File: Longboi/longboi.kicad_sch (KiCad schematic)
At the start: 192 parts, among them J2 ICSP_Header, K0 KEYSW, K1 KEYSW, K10 KEYSW, K11 KEYSW, K12 KEYSW, K13 KEYSW, K14 KEYSW, K15 KEYSW, K16 KEYSW, K17 KEYSW, K18 KEYSW, K19 KEYSW, K2 KEYSW, K20 KEYSW, K21 KEYSW, K22 KEYSW, K22-spacer1 KEYSW, K22-stepped1 KEYSW, K23 KEYSW, K24 KEYSW, K25 KEYSW, K26 KEYSW, K27 KEYSW, K28 KEYSW, K29 KEYSW, K3 KEYSW, K3-2uVert1 KEYSW, K30 KEYSW, K31 KEYSW, K32 KEYSW, K33 KEYSW, K34 KEYSW, K35 KEYSW, K36 KEYSW, K37 KEYSW, K38 KEYSW, K38-2uVert1 KEYSW, K39 KEYSW, K39-spacer1 KEYSW, K4 KEYSW, K4-spacer1 KEYSW, K40 KEYSW, K41 KEYSW, K42 KEYSW, K43 KEYSW, K44 KEYSW, K45 KEYSW, K46 KEYSW, K47 KEYSW, K48 KEYSW, K49 KEYSW, K5 KEYSW, K50 KEYSW, K51 KEYSW, K52 KEYSW, K52-1u1 KEYSW, K52-2u1 KEYSW, K53 KEYSW, K54 KEYSW, K55 KEYSW, K55-1.25 KEYSW, K55-spacer1 KEYSW, K56 KEYSW, K56-1.25 KEYSW, K57 KEYSW, K57-1.25 KEYSW, K57-1.5u1 KEYSW, K57-1u1 KEYSW, K58 KEYSW, K58-6u1 KEYSW, K58for1.25Row1 KEYSW, K59 KEYSW, K59-1.25u1 KEYSW, K59-7u1 KEYSW, K59Alt1 KEYSW, K6 KEYSW, K60 KEYSW, K60Alt1 KEYSW, K61 KEYSW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

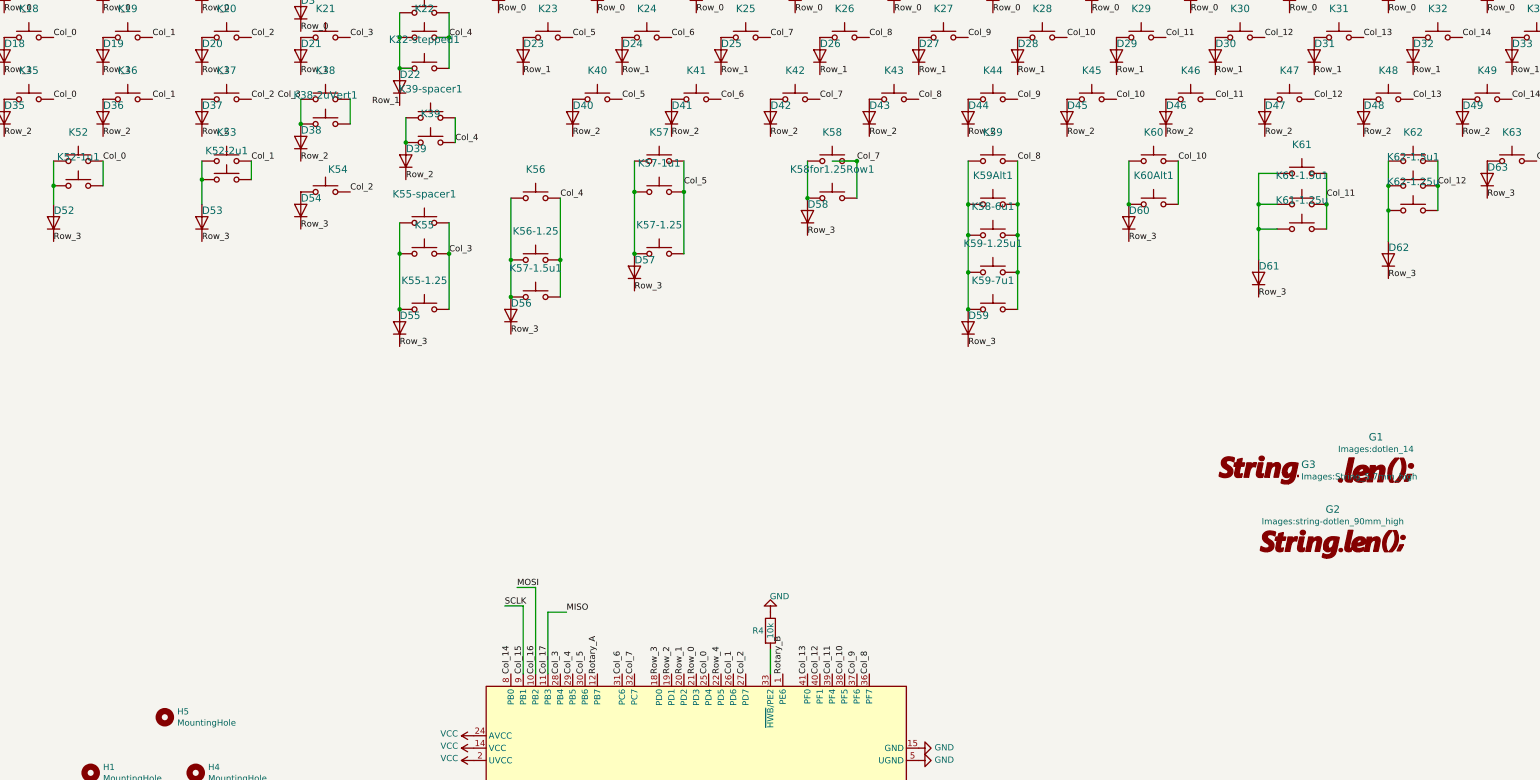
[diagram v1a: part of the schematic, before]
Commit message: fix bug in longboi...
key38 was not schematiced right
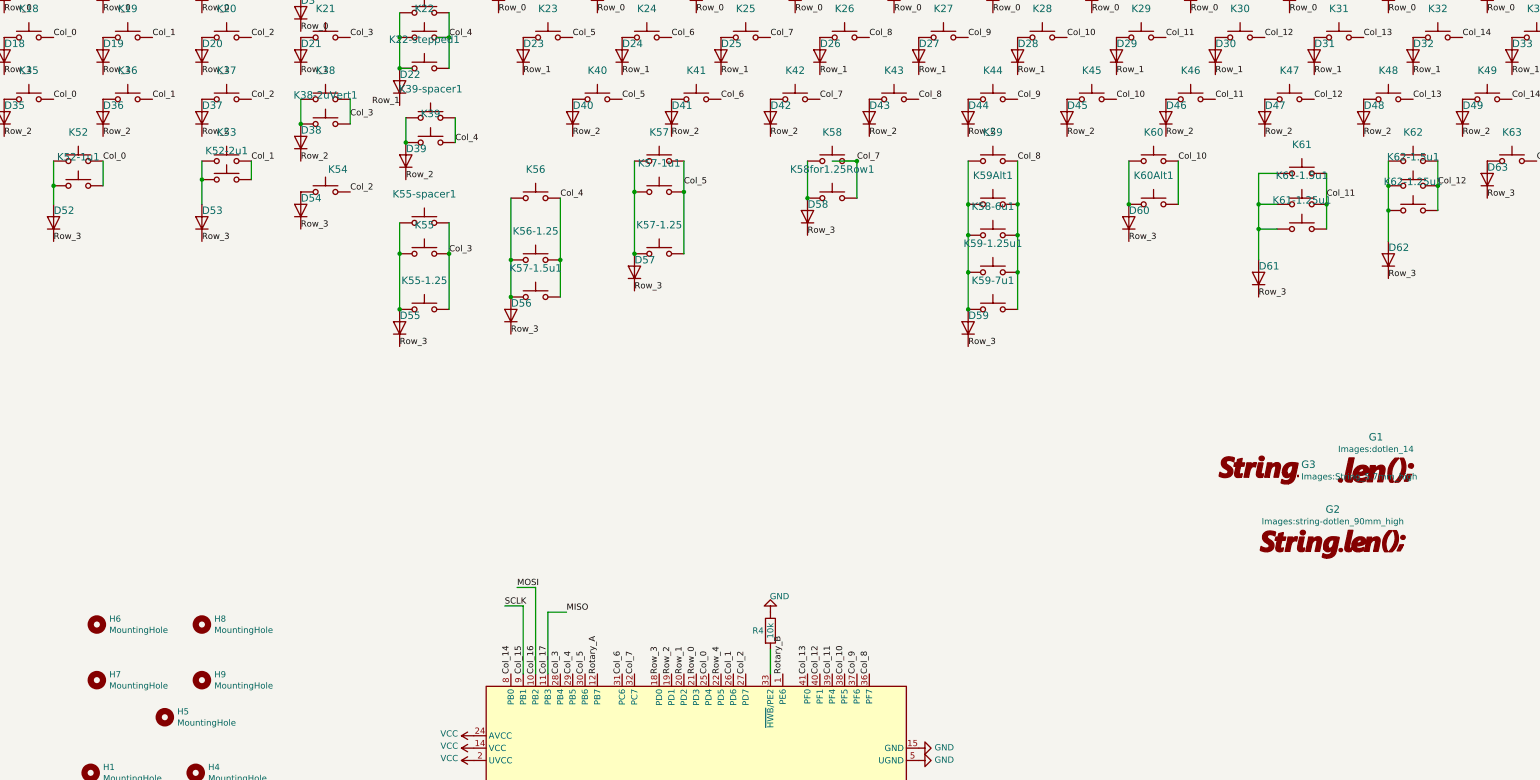
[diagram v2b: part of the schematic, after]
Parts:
- added H6, H7, H8, H9: MountingHole, random-keyboard-parts:M2 Mounting Hole, symbol Mechanical:MountingHole
- renumbered K61-1.25u to K61-1.25u1, K62-1.25u to K62-1.25u1
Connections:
- net Col_3: now also K38-2uVert1.2, K38.2; no longer D38.2 (A), K38-2uVert1.1, K38.1
- new net: D38.2 (A), K38-2uVert1.1, K38.1
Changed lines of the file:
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@@
   (junction (at 185.42 90.17) (diameter 0) (color 0 0 0 0)
   )
-  (junction (at 81.28 74.93) (diameter 0) (color 0 0 0 0)
-  )
   (junction (at 111.76 101.6) (diameter 0) (color 0 0 0 0)
   )
@@
   (junction (at 69.85 242.57) (diameter 0) (color 0 0 0 0)
   )
+  (junction (at 81.28 74.93) (diameter 0) (color 0 0 0 0)
+  )
   (junction (at 251.46 91.44) (diameter 0) (color 0 0 0 0)
   )
@@
     (stroke (width 0) (type default) (color 0 0 0 0))
   )
-  (wire (pts (xy 81.28 69.85) (xy 81.28 74.93))
-    (stroke (width 0) (type default) (color 0 0 0 0))
-  )
   (wire (pts (xy 190.5 82.55) (xy 195.58 82.55))
     (stroke (width 0) (type default) (color 0 0 0 0))
@@
     (stroke (width 0) (type default) (color 0 0 0 0))
   )
+  (wire (pts (xy 81.28 69.85) (xy 81.28 74.93))
+    (stroke (width 0) (type default) (color 0 0 0 0))
+  )
   (wire (pts (xy 394.97 36.83) (xy 403.86 36.83))
     (stroke (width 0) (type default) (color 0 0 0 0))
@@
     (effects (font (size 1.27 1.27)) (justify left bottom))
   )
-  (label "Col_3" (at 81.28 69.85 180)
-    (effects (font (size 1.27 1.27)) (justify right bottom))
+  (label "Col_3" (at 91.44 73.66 0)
+    (effects (font (size 1.27 1.27)) (justify left bottom))
   )
   (label "Row_1" (at 269.24 64.77 0)
@@
     (pin "2")
   )
+  (symbol (lib_id "Mechanical:MountingHole") (at 39.37 189.23 0) (unit 1)
+    (in_bom yes) (on_board yes)
+    (property "Reference" "H7" (id 0) (at 41.91 188.0616 0)
+      (effects (font (size 1.27 1.27)) (justify left))
+    )
+    (property "Value" "MountingHole" (id 1) (at 41.91 190.373 0)
+      (effects (font (size 1.27 1.27)) (justify left))
+    )
+    (property "Footprint" "random-keyboard-parts:M2 Mounting Hole" (id 2) (at 39.37 189.23 0)
+      (effects (font (size 1.27 1.27)) hide)
+    )
+    (property "Datasheet" "~" (id 3) (at 39.37 189.23 0)
+      (effects (font (size 1.27 1.27)) hide)
+    )
+  )
+  (symbol (lib_id "Mechanical:MountingHole") (at 60.96 177.8 0) (unit 1)
+    (in_bom yes) (on_board yes)
+    (property "Reference" "H8" (id 0) (at 63.5 176.6316 0)
+      (effects (font (size 1.27 1.27)) (justify left))
+    )
+    (property "Value" "MountingHole" (id 1) (at 63.5 178.943 0)
+      (effects (font (size 1.27 1.27)) (justify left))
+    )
+    (property "Footprint" "random-keyboard-parts:M2 Mounting Hole" (id 2) (at 60.96 177.8 0)
+      (effects (font (size 1.27 1.27)) hide)
+    )
+    (property "Datasheet" "~" (id 3) (at 60.96 177.8 0)
+      (effects (font (size 1.27 1.27)) hide)
+    )
+  )
+  (symbol (lib_id "Mechanical:MountingHole") (at 60.96 189.23 0) (unit 1)
+    (in_bom yes) (on_board yes)
+    (property "Reference" "H9" (id 0) (at 63.5 188.0616 0)
+      (effects (font (size 1.27 1.27)) (justify left))
+    )
+    (property "Value" "MountingHole" (id 1) (at 63.5 190.373 0)
+      (effects (font (size 1.27 1.27)) (justify left))
+    )
+    (property "Footprint" "random-keyboard-parts:M2 Mounting Hole" (id 2) (at 60.96 189.23 0)
+      (effects (font (size 1.27 1.27)) hide)
+    )
+    (property "Datasheet" "~" (id 3) (at 60.96 189.23 0)
+      (effects (font (size 1.27 1.27)) hide)
+    )
+  )
   (symbol (lib_id "Switch:SW_Push") (at 309.88 92.71 0) (unit 1)
     (in_bom yes) (on_board yes)
-    (property "Reference" "K62-1.25u" (id 0) (at 309.88 86.7918 0)
+    (property "Reference" "K62-1.25u1" (id 0) (at 309.88 86.7918 0)
       (effects (font (size 1.524 1.524)))
     )
@@
   (symbol (lib_id "Switch:SW_Push") (at 287.02 96.52 0) (unit 1)
     (in_bom yes) (on_board yes)
-    (property "Reference" "K61-1.25u" (id 0) (at 287.02 90.6018 0)
+    (property "Reference" "K61-1.25u1" (id 0) (at 287.02 90.6018 0)
       (effects (font (size 1.524 1.524)))
     )
@@
     (pin "2")
   )
+  (symbol (lib_id "Mechanical:MountingHole") (at 39.37 177.8 0) (unit 1)
+    (in_bom yes) (on_board yes)
+    (property "Reference" "H6" (id 0) (at 41.91 176.6316 0)
+      (effects (font (size 1.27 1.27)) (justify left))
+    )
+    (property "Value" "MountingHole" (id 1) (at 41.91 178.943 0)
+      (effects (font (size 1.27 1.27)) (justify left))
+    )
+    (property "Footprint" "random-keyboard-parts:M2 Mounting Hole" (id 2) (at 39.37 177.8 0)
+      (effects (font (size 1.27 1.27)) hide)
+    )
+    (property "Datasheet" "~" (id 3) (at 39.37 177.8 0)
+      (effects (font (size 1.27 1.27)) hide)
+    )
+  )
   (symbol (lib_id "Switch:SW_Push") (at 66.04 86.36 0) (unit 1)
     (in_bom yes) (on_board yes)
@@
       (reference "H5") (unit 1) (value "MountingHole") (footprint "random-keyboard-parts:M2 Mounting Hole")
     )
+    (path "/e0ffc4a5-acee-444d-9091-cb09a2fd596a"
+      (reference "H6") (unit 1) (value "MountingHole") (footprint "random-keyboard-parts:M2 Mounting Hole")
+    )
+    (path "/10fcbf2d-6552-4910-ae9e-906304f0e093"
+      (reference "H7") (unit 1) (value "MountingHole") (footprint "random-keyboard-parts:M2 Mounting Hole")
+    )
+    (path "/339b77fe-16f3-43b4-8399-7230a8ae2102"
+      (reference "H8") (unit 1) (value "MountingHole") (footprint "random-keyboard-parts:M2 Mounting Hole")
+    )
+    (path "/3427d123-61e2-4c57-80e1-efb5d2751d47"
+      (reference "H9") (unit 1) (value "MountingHole") (footprint "random-keyboard-parts:M2 Mounting Hole")
+    )
     (path "/00000000-0000-0000-0000-000062166a49"
       (reference "J2") (unit 1) (value "ICSP_Header") (footprint "Connector_PinHeader_2.54mm:PinHeader_2x03_P2.54mm_Vertical")
@@
     )
     (path "/94c26993-bb91-483b-ab9b-cc98b43c45dd"
-      (reference "K61-1.25u") (unit 1) (value "KEYSW") (footprint "MX_Only:MXOnly-1.25U-NoLED")
+      (reference "K61-1.25u1") (unit 1) (value "KEYSW") (footprint "MX_Only:MXOnly-1.25U-NoLED")
     )
     (path "/00000000-0000-0000-0000-000062166a78"
@@
     )
     (path "/710abe27-ce29-434f-9460-1c18893d781d"
-      (reference "K62-1.25u") (unit 1) (value "KEYSW") (footprint "MX_Only:MXOnly-1.25U-NoLED")
+      (reference "K62-1.25u1") (unit 1) (value "KEYSW") (footprint "MX_Only:MXOnly-1.25U-NoLED")
     )
     (path "/00000000-0000-0000-0000-000062166a74"

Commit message: clean up map and string with prototype fixes
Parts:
- added D70: SOD-323F, Diode_SMD:D_SOD-323F, symbol Device:D
- added K55-spacer2, K70: KEYSW, MX_Only:MXOnly-1U-NoLED, symbol Switch:SW_Push
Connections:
- net Col_1: now also K70.2; no longer K52-2u1.2, K53.2
- net Col_2: now also K52-2u1.2, K53.2; no longer K54.2
- net Col_3: now also K54.2; no longer K55-1.25.2, K55-spacer1.2, K55.2
- net Col_4: now also K55-1.25.2, K55-spacer1.2, K55.2, K55-spacer2.2; no longer K56-1.25.2, K56.2, K57-1.5u1.2
- net Col_5: now also K56-1.25.2, K56.2, K57-1.5u1.2; no longer K57-1.25.2, K57-1u1.2, K57.2
- net Col_6: now also K57-1.25.2, K57-1u1.2, K57.2
- net Row_3: now also D70.1 (K)
- net at D55.2 (A), K55-1.25.1, K55-spacer1.1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: now also K55-spacer2.1
- new net: D70.2 (A), K70.1
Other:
- moved on the sheet: D0, D1, D10, D11, D12, D13, D14, D15, D16, D17, D18, D19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

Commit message: moreupdates to tweak the two keyboards
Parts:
- removed K52-2u1: KEYSW, MX_Only:MXOnly-2U-ReversedStabilizers-NoLED, symbol Switch:SW_Push
- added K0-2uVert1, K35-2uVert1: KEYSW, MX_Only:MXOnly-2U-NoLED, symbol Switch:SW_Push
- added K54-2u1, K70-2u1: KEYSW, MX_Only:MXOnly-2U-ReversedStabilizers-NoLED, symbol Switch:SW_Push
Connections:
- net Col_0: now also K0-2uVert1.2, K35-2uVert1.2
- net Col_1: now also K70-2u1.2
- net Col_3: now also K54-2u1.2
- net at D54.2 (A), K54.1: now also K54-2u1.1
- net at D35.2 (A), K35.1: now also K35-2uVert1.1
- net at D0.2 (A), K0.1: now also K0-2uVert1.1
- net at D70.2 (A), K70.1: now also K70-2u1.1
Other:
- moved on the sheet: K53
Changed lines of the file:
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@@
   (junction (at 342.9 40.64) (diameter 0) (color 0 0 0 0)
   )
+  (junction (at 20.32 33.02) (diameter 0) (color 0 0 0 0)
+  )
   (junction (at 242.57 102.87) (diameter 0) (color 0 0 0 0)
   )
@@
   (junction (at 287.02 142.24) (diameter 0) (color 0 0 0 0)
   )
+  (junction (at 63.5 148.59) (diameter 0) (color 0 0 0 0)
+  )
   (junction (at 104.14 156.21) (diameter 0) (color 0 0 0 0)
   )
+  (junction (at 104.14 148.59) (diameter 0) (color 0 0 0 0)
+  )
   (junction (at 167.64 135.89) (diameter 0) (color 0 0 0 0)
   )
@@
   (junction (at 63.5 156.21) (diameter 0) (color 0 0 0 0)
   )
+  (junction (at 33.02 95.25) (diameter 0) (color 0 0 0 0)
+  )
   (junction (at 163.83 78.74) (diameter 0) (color 0 0 0 0)
   )
@@
   (junction (at 123.19 247.65) (diameter 0) (color 0 0 0 0)
   )
-  (junction (at 86.36 143.51) (diameter 0) (color 0 0 0 0)
-  )
   (junction (at 204.47 78.74) (diameter 0) (color 0 0 0 0)
   )
@@
     (stroke (width 0) (type default) (color 0 0 0 0))
   )
+  (wire (pts (xy 114.3 146.05) (xy 114.3 148.59))
+    (stroke (width 0) (type default) (color 0 0 0 0))
+  )
   (wire (pts (xy 241.3 156.21) (xy 260.35 156.21))
     (stroke (width 0) (type default) (color 0 0 0 0))
@@
     (stroke (width 0) (type default) (color 0 0 0 0))
   )
+  (wire (pts (xy 63.5 146.05) (xy 63.5 148.59))
+    (stroke (width 0) (type default) (color 0 0 0 0))
+  )
   (wire (pts (xy 213.36 118.11) (xy 213.36 127))
     (stroke (width 0) (type default) (color 0 0 0 0))
@@
     (stroke (width 0) (type default) (color 0 0 0 0))
   )
+  (wire (pts (xy 30.48 29.21) (xy 30.48 33.02))
+    (stroke (width 0) (type default) (color 0 0 0 0))
+  )
   (wire (pts (xy 204.47 78.74) (xy 224.79 78.74))
     (stroke (width 0) (type default) (color 0 0 0 0))
@@
     (stroke (width 0) (type default) (color 0 0 0 0))
   )
-  (wire (pts (xy 86.36 148.59) (xy 86.36 143.51))
+  (wire (pts (xy 86.36 146.05) (xy 86.36 148.59))
     (stroke (width 0) (type default) (color 0 0 0 0))
   )
@@
     (stroke (width 0) (type default) (color 0 0 0 0))
   )
+  (wire (pts (xy 20.32 29.21) (xy 20.32 33.02))
+    (stroke (width 0) (type default) (color 0 0 0 0))
+  )
   (wire (pts (xy 394.97 33.02) (xy 394.97 36.83))
     (stroke (width 0) (type default) (color 0 0 0 0))
@@
     (stroke (width 0) (type default) (color 0 0 0 0))
   )
-  (wire (pts (xy 96.52 139.7) (xy 96.52 143.51))
-    (stroke (width 0) (type default) (color 0 0 0 0))
-  )
   (wire (pts (xy 102.87 59.69) (xy 102.87 64.77))
     (stroke (width 0) (type default) (color 0 0 0 0))
@@
     (stroke (width 0) (type default) (color 0 0 0 0))
   )
+  (wire (pts (xy 73.66 146.05) (xy 73.66 148.59))
+    (stroke (width 0) (type default) (color 0 0 0 0))
+  )
   (wire (pts (xy 331.47 156.21) (xy 351.79 156.21))
     (stroke (width 0) (type default) (color 0 0 0 0))
@@
     (stroke (width 0) (type default) (color 0 0 0 0))
   )
+  (wire (pts (xy 43.18 91.44) (xy 43.18 95.25))
+    (stroke (width 0) (type default) (color 0 0 0 0))
+  )
   (wire (pts (xy 241.3 148.59) (xy 241.3 139.7))
     (stroke (width 0) (type default) (color 0 0 0 0))
@@
     (stroke (width 0) (type default) (color 0 0 0 0))
   )
+  (wire (pts (xy 104.14 146.05) (xy 104.14 148.59))
+    (stroke (width 0) (type default) (color 0 0 0 0))
+  )
   (wire (pts (xy 403.86 21.59) (xy 384.81 21.59))
     (stroke (width 0) (type default) (color 0 0 0 0))
@@
     (stroke (width 0) (type default) (color 0 0 0 0))
   )
-  (wire (pts (xy 86.36 143.51) (xy 86.36 139.7))
-    (stroke (width 0) (type default) (color 0 0 0 0))
-  )
   (wire (pts (xy 403.86 30.48) (xy 403.86 21.59))
     (stroke (width 0) (type default) (color 0 0 0 0))
@@
     (stroke (width 0) (type default) (color 0 0 0 0))
   )
+  (wire (pts (xy 33.02 91.44) (xy 33.02 95.25))
+    (stroke (width 0) (type default) (color 0 0 0 0))
+  )
   (wire (pts (xy 129.54 170.18) (xy 125.73 170.18))
     (stroke (width 0) (type default) (color 0 0 0 0))
@@
     (effects (font (size 1.27 1.27)) (justify left bottom))
   )
-  (label "Col_2" (at 96.52 139.7 0)
+  (label "Col_2" (at 96.52 146.05 0)
     (effects (font (size 1.27 1.27)) (justify left bottom))
   )
@@
     (pin "2")
   )
-  (symbol (lib_id "Switch:SW_Push") (at 91.44 139.7 0) (unit 1)
+  (symbol (lib_id "Switch:SW_Push") (at 91.44 146.05 0) (unit 1)
     (in_bom yes) (on_board yes)
-    (property "Reference" "K53" (id 0) (at 91.44 133.7818 0)
+    (property "Reference" "K53" (id 0) (at 91.44 140.1318 0)
       (effects (font (size 1.524 1.524)))
     )
-    (property "Value" "KEYSW" (id 1) (at 91.44 142.24 0)
+    (property "Value" "KEYSW" (id 1) (at 91.44 148.59 0)
       (effects (font (size 1.524 1.524)) hide)
     )
-    (property "Footprint" "MX_Only:MXOnly-1U-NoLED" (id 2) (at 91.44 139.7 0)
+    (property "Footprint" "MX_Only:MXOnly-1U-NoLED" (id 2) (at 91.44 146.05 0)
       (effects (font (size 1.524 1.524)) hide)
     )
-    (property "Datasheet" "" (id 3) (at 91.44 139.7 0)
+    (property "Datasheet" "" (id 3) (at 91.44 146.05 0)
       (effects (font (size 1.524 1.524)))
     )
@@
     )
   )
+  (symbol (lib_id "Switch:SW_Push") (at 68.58 146.05 0) (unit 1)
+    (in_bom yes) (on_board yes)
+    (property "Reference" "K70-2u1" (id 0) (at 68.58 140.1318 0)
+      (effects (font (size 1.524 1.524)))
+    )
+    (property "Value" "KEYSW" (id 1) (at 68.58 148.59 0)
+      (effects (font (size 1.524 1.524)) hide)
+    )
+    (property "Footprint" "MX_Only:MXOnly-2U-ReversedStabilizers-NoLED" (id 2) (at 68.58 146.05 0)
+      (effects (font (size 1.524 1.524)) hide)
+    )
+    (property "Datasheet" "" (id 3) (at 68.58 146.05 0)
+      (effects (font (size 1.524 1.524)))
+    )
+    (pin "1")
+    (pin "2")
+  )
   (symbol (lib_id "Switch:SW_Push") (at 292.1 142.24 0) (unit 1)
     (in_bom yes) (on_board yes)
@@
     (pin "2")
   )
+  (symbol (lib_id "Switch:SW_Push") (at 25.4 29.21 0) (unit 1)
+    (in_bom yes) (on_board yes)
+    (property "Reference" "K0-2uVert1" (id 0) (at 25.4 23.2918 0)
+      (effects (font (size 1.524 1.524)))
+    )
+    (property "Value" "KEYSW" (id 1) (at 25.4 31.75 0)
+      (effects (font (size 1.524 1.524)) hide)
+    )
+    (property "Footprint" "MX_Only:MXOnly-2U-NoLED" (id 2) (at 25.4 29.21 0)
+      (effects (font (size 1.524 1.524)) hide)
+    )
+    (property "Datasheet" "" (id 3) (at 25.4 29.21 0)
+      (effects (font (size 1.524 1.524)))
+    )
+    (pin "1")
+    (pin "2")
+  )
+  (symbol (lib_id "Switch:SW_Push") (at 38.1 91.44 0) (unit 1)
+    (in_bom yes) (on_board yes)
+    (property "Reference" "K35-2uVert1" (id 0) (at 38.1 87.63 0)
+      (effects (font (size 1.524 1.524)))
+    )
+    (property "Value" "KEYSW" (id 1) (at 38.1 93.98 0)
+      (effects (font (size 1.524 1.524)) hide)
+    )
+    (property "Footprint" "MX_Only:MXOnly-2U-NoLED" (id 2) (at 38.1 91.44 0)
+      (effects (font (size 1.524 1.524)) hide)
+    )
+    (property "Datasheet" "" (id 3) (at 38.1 91.44 0)
+      (effects (font (size 1.524 1.524)))
+    )
+    (pin "1")
+    (pin "2")
+  )
   (symbol (lib_id "Mechanical:MountingHole") (at 39.37 177.8 0) (unit 1)
     (in_bom yes) (on_board yes)
@@
     )
   )
-  (symbol (lib_id "Switch:SW_Push") (at 91.44 143.51 0) (unit 1)
+  (symbol (lib_id "Switch:SW_Push") (at 109.22 146.05 0) (unit 1)
     (in_bom yes) (on_board yes)
-    (property "Reference" "K52-2u1" (id 0) (at 91.44 137.5918 0)
+    (property "Reference" "K54-2u1" (id 0) (at 109.22 140.1318 0)
       (effects (font (size 1.524 1.524)))
     )
-    (property "Value" "KEYSW" (id 1) (at 91.44 146.05 0)
+    (property "Value" "KEYSW" (id 1) (at 109.22 148.59 0)
       (effects (font (size 1.524 1.524)) hide)
     )
-    (property "Footprint" "MX_Only:MXOnly-2U-ReversedStabilizers-NoLED" (id 2) (at 91.44 143.51 0)
+    (property "Footprint" "MX_Only:MXOnly-2U-ReversedStabilizers-NoLED" (id 2) (at 109.22 146.05 0)
       (effects (font (size 1.524 1.524)) hide)
     )
-    (property "Datasheet" "" (id 3) (at 91.44 143.51 0)
+    (property "Datasheet" "" (id 3) (at 109.22 146.05 0)
       (effects (font (size 1.524 1.524)))
     )
@@
       (reference "K0") (unit 1) (value "KEYSW") (footprint "MX_Only:MXOnly-1U-NoLED")
     )
+    (path "/b6892239-8cc4-4239-9f6b-bd2be89fdd6c"
+      (reference "K0-2uVert1") (unit 1) (value "KEYSW") (footprint "MX_Only:MXOnly-2U-NoLED")
+    )
     (path "/00000000-0000-0000-0000-000062166a86"
       (reference "K1") (unit 1) (value "KEYSW") (footprint "MX_Only:MXOnly-1U-NoLED")
@@
       (reference "K35") (unit 1) (value "KEYSW") (footprint "MX_Only:MXOnly-1U-NoLED")
     )
+    (path "/d631fecf-1e8a-41e4-b2c3-fff52c91425c"
+      (reference "K35-2uVert1") (unit 1) (value "KEYSW") (footprint "MX_Only:MXOnly-2U-NoLED")
+    )
     (path "/00000000-0000-0000-0000-000062166a6c"
       (reference "K36") (unit 1) (value "KEYSW") (footprint "MX_Only:MXOnly-1U-NoLED")
@@
       (reference "K52-1u1") (unit 1) (value "KEYSW") (footprint "MX_Only:MXOnly-1U-NoLED")
     )
-    (path "/f30c2f0a-f4f0-45a3-9cc7-98d3fd524f81"
-      (reference "K52-2u1") (unit 1) (value "KEYSW") (footprint "MX_Only:MXOnly-2U-ReversedStabilizers-NoLED")
-    )
     (path "/00000000-0000-0000-0000-000062166a54"
       (reference "K53") (unit 1) (value "KEYSW") (footprint "MX_Only:MXOnly-1U-NoLED")
@@
       (reference "K54") (unit 1) (value "KEYSW") (footprint "MX_Only:MXOnly-1U-NoLED")
     )
+    (path "/e6a2b5b5-3723-48bf-9f47-7b6134ec2638"
+      (reference "K54-2u1") (unit 1) (value "KEYSW") (footprint "MX_Only:MXOnly-2U-ReversedStabilizers-NoLED")
+    )
     (path "/00000000-0000-0000-0000-000062166a5a"
       (reference "K55") (unit 1) (value "KEYSW") (footprint "MX_Only:MXOnly-1.5U-NoLED")
@@
       (reference "K70") (unit 1) (value "KEYSW") (footprint "MX_Only:MXOnly-1U-NoLED")
     )
+    (path "/4da99aa8-1be4-4f00-a5f9-92db63e2b689"
+      (reference "K70-2u1") (unit 1) (value "KEYSW") (footprint "MX_Only:MXOnly-2U-ReversedStabilizers-NoLED")
+    )
     (path "/00000000-0000-0000-0000-000061fcf0d7"
